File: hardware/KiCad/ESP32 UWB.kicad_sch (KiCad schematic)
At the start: 55 parts, among them J1 HEADER-20P-2.54, J2 HEADER-12P-2.54, J3 10118194-0001LF, Q1 S8050, Q2 S8050, SW1 BUTTON, SW2 BUTTON, U1 AMS1117-3.3, U2 ESP32-C3-MINI-1-N4, U3 SILICON_LABS_CP2102N-A01-GQFN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

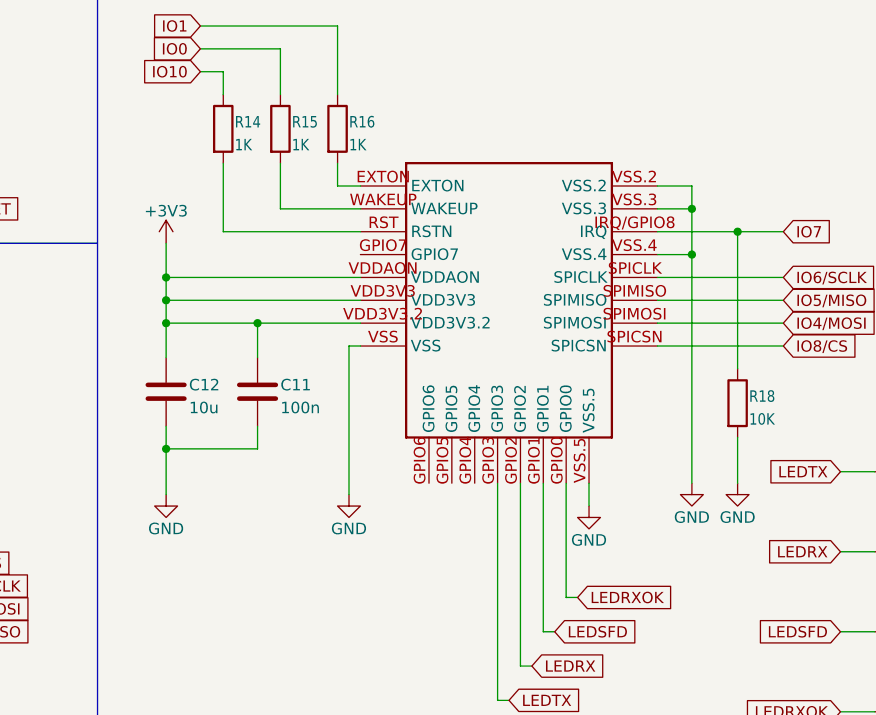
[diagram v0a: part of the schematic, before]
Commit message: further cleanup and improvment of the KiCad version of the PCB
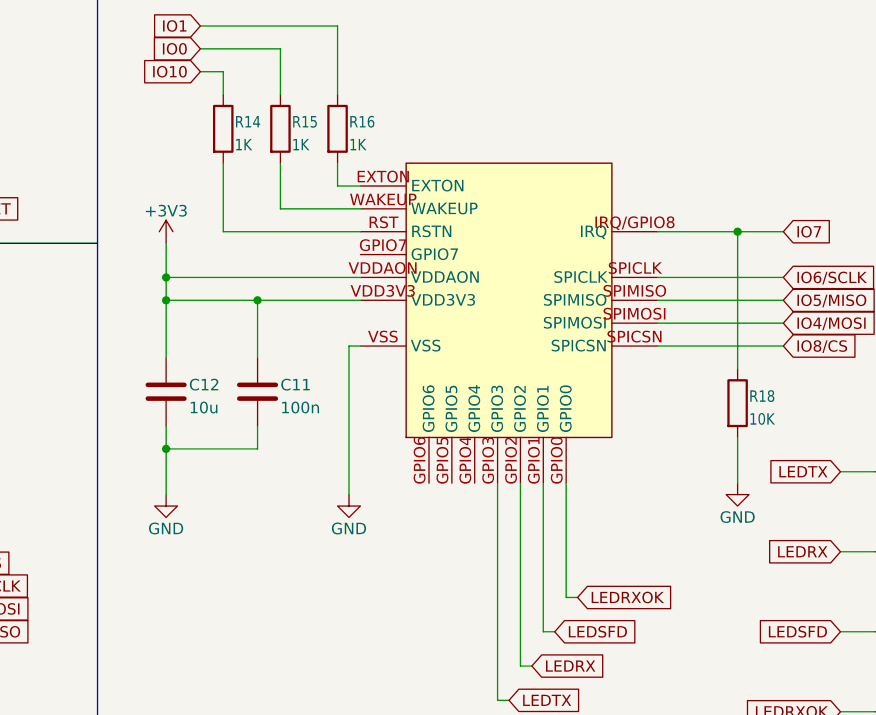
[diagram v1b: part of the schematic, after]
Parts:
- SW1, SW2: footprint Button_Switch_SMD:SW_SPST_EVQPE1 -> ESP32 UWB:SW_Push_3x4mm
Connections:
- net +3V3: no longer U4.VDD3V3.2
- net GND: no longer U4.VSS.2, U4.VSS.3, U4.VSS.4, U4.VSS.5
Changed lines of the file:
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@@
   (junction (at 173.99 123.19) (diameter 0) (color 0 0 0 0)
   )
-  (junction (at 297.18 135.89) (diameter 0) (color 0 0 0 0)
-  )
   (junction (at 146.05 171.45) (diameter 0) (color 0 0 0 0)
   )
@@
   (junction (at 151.13 41.91) (diameter 0) (color 0 0 0 0)
   )
-  (junction (at 238.76 146.05) (diameter 0) (color 0 0 0 0)
-  )
   (junction (at 193.04 113.03) (diameter 0) (color 0 0 0 0)
   )
@@
   (junction (at 173.99 107.95) (diameter 0) (color 0 0 0 0)
   )
-  (junction (at 238.76 148.59) (diameter 0) (color 0 0 0 0)
+  (junction (at 238.76 146.05) (diameter 0) (color 0 0 0 0)
   )
   (junction (at 316.23 50.8) (diameter 0) (color 0 0 0 0)
@@
   (junction (at 243.84 38.1) (diameter 0) (color 0 0 0 0)
   )
-  (junction (at 297.18 140.97) (diameter 0) (color 0 0 0 0)
-  )
   (junction (at 140.97 127) (diameter 0) (color 0 0 0 0)
   )
@@
   (junction (at 173.99 105.41) (diameter 0) (color 0 0 0 0)
   )
-  (junction (at 248.92 148.59) (diameter 0) (color 0 0 0 0)
+  (junction (at 248.92 146.05) (diameter 0) (color 0 0 0 0)
   )
   (junction (at 146.05 158.75) (diameter 0) (color 0 0 0 0)
@@
     (stroke (width 0) (type default) (color 0 0 0 0))
   )
-  (wire (pts (xy 238.76 152.4) (xy 238.76 148.59))
+  (wire (pts (xy 238.76 152.4) (xy 238.76 146.05))
     (stroke (width 0) (type default) (color 0 0 0 0))
   )
@@
     (stroke (width 0) (type default) (color 0 0 0 0))
   )
-  (wire (pts (xy 293.37 140.97) (xy 297.18 140.97))
-    (stroke (width 0) (type default) (color 0 0 0 0))
-  )
   (wire (pts (xy 161.29 110.49) (xy 173.99 110.49))
     (stroke (width 0) (type default) (color 0 0 0 0))
@@
     (stroke (width 0) (type default) (color 0 0 0 0))
   )
-  (wire (pts (xy 248.92 152.4) (xy 248.92 148.59))
+  (wire (pts (xy 248.92 152.4) (xy 248.92 146.05))
     (stroke (width 0) (type default) (color 0 0 0 0))
   )
@@
     (stroke (width 0) (type default) (color 0 0 0 0))
   )
-  (wire (pts (xy 238.76 146.05) (xy 238.76 143.51))
-    (stroke (width 0) (type default) (color 0 0 0 0))
-  )
   (wire (pts (xy 189.23 113.03) (xy 193.04 113.03))
     (stroke (width 0) (type default) (color 0 0 0 0))
@@
     (stroke (width 0) (type default) (color 0 0 0 0))
   )
-  (wire (pts (xy 297.18 140.97) (xy 297.18 135.89))
-    (stroke (width 0) (type default) (color 0 0 0 0))
-  )
   (wire (pts (xy 161.29 74.93) (xy 177.8 74.93))
     (stroke (width 0) (type default) (color 0 0 0 0))
@@
     (stroke (width 0) (type default) (color 0 0 0 0))
   )
-  (wire (pts (xy 238.76 148.59) (xy 248.92 148.59))
+  (wire (pts (xy 238.76 146.05) (xy 248.92 146.05))
     (stroke (width 0) (type default) (color 0 0 0 0))
   )
@@
     (stroke (width 0) (type default) (color 0 0 0 0))
   )
-  (wire (pts (xy 293.37 135.89) (xy 297.18 135.89))
-    (stroke (width 0) (type default) (color 0 0 0 0))
-  )
-  (wire (pts (xy 260.35 148.59) (xy 248.92 148.59))
-    (stroke (width 0) (type default) (color 0 0 0 0))
-  )
   (wire (pts (xy 302.26 138.43) (xy 302.26 153.67))
     (stroke (width 0) (type default) (color 0 0 0 0))
@@
     (stroke (width 0) (type default) (color 0 0 0 0))
   )
-  (wire (pts (xy 293.37 133.35) (xy 297.18 133.35))
-    (stroke (width 0) (type default) (color 0 0 0 0))
-  )
   (wire (pts (xy 308.61 71.12) (xy 317.5 71.12))
     (stroke (width 0) (type default) (color 0 0 0 0))
@@
     (stroke (width 0) (type default) (color 0 0 0 0))
   )
+  (wire (pts (xy 248.92 146.05) (xy 260.35 146.05))
+    (stroke (width 0) (type default) (color 0 0 0 0))
+  )
   (wire (pts (xy 199.39 77.47) (xy 215.9 77.47))
     (stroke (width 0) (type default) (color 0 0 0 0))
@@
     (stroke (width 0) (type default) (color 0 0 0 0))
   )
-  (wire (pts (xy 238.76 146.05) (xy 260.35 146.05))
-    (stroke (width 0) (type default) (color 0 0 0 0))
-  )
   (wire (pts (xy 259.08 151.13) (xy 260.35 151.13))
     (stroke (width 0) (type default) (color 0 0 0 0))
@@
     (stroke (width 0) (type default) (color 0 0 0 0))
   )
-  (wire (pts (xy 285.75 166.37) (xy 285.75 168.91))
-    (stroke (width 0) (type default) (color 0 0 0 0))
-  )
   (wire (pts (xy 85.09 160.02) (xy 97.79 160.02))
     (stroke (width 0) (type default) (color 0 0 0 0))
@@
     (stroke (width 0) (type default) (color 0 0 0 0))
   )
-  (wire (pts (xy 297.18 140.97) (xy 297.18 166.37))
-    (stroke (width 0) (type default) (color 0 0 0 0))
-  )
   (wire (pts (xy 251.46 135.89) (xy 260.35 135.89))
     (stroke (width 0) (type default) (color 0 0 0 0))
@@
     (stroke (width 0) (type default) (color 0 0 0 0))
   )
-  (wire (pts (xy 238.76 148.59) (xy 238.76 146.05))
+  (wire (pts (xy 238.76 143.51) (xy 238.76 146.05))
     (stroke (width 0) (type default) (color 0 0 0 0))
   )
@@
     (stroke (width 0) (type default) (color 0 0 0 0))
   )
-  (wire (pts (xy 297.18 135.89) (xy 297.18 133.35))
-    (stroke (width 0) (type default) (color 0 0 0 0))
-  )
   (wire (pts (xy 129.54 180.34) (xy 129.54 186.69))
     (stroke (width 0) (type default) (color 0 0 0 0))
@@
       (effects (font (size 1.778 1.5113)) (justify left bottom))
     )
-    (property "Footprint" "Button_Switch_SMD:SW_SPST_EVQPE1" (id 2) (at 102.87 173.99 0)
+    (property "Footprint" "ESP32 UWB:SW_Push_3x4mm" (id 2) (at 102.87 173.99 0)
       (effects (font (size 1.27 1.27)) hide)
     )
@@
       (effects (font (size 1.778 1.5113)) (justify left bottom))
     )
-    (property "Footprint" "Button_Switch_SMD:SW_SPST_EVQPE1" (id 2) (at 102.87 160.02 0)
+    (property "Footprint" "ESP32 UWB:SW_Push_3x4mm" (id 2) (at 102.87 160.02 0)
       (effects (font (size 1.27 1.27)) hide)
     )
@@
     (pin "SPIMOSI")
     (pin "VDD3V3")
-    (pin "VDD3V3.2")
     (pin "VDDAON")
     (pin "VSS")
-    (pin "VSS.2")
-    (pin "VSS.3")
-    (pin "VSS.4")
-    (pin "VSS.5")
     (pin "WAKEUP")
   )
@@
     (pin "1")
   )
-  (symbol (lib_id "power:GND") (at 285.75 168.91 0) (unit 1)
-    (in_bom yes) (on_board yes)
-    (property "Reference" "#PWR0112" (id 0) (at 285.75 175.26 0)
-      (effects (font (size 1.27 1.27)) hide)
-    )
-    (property "Value" "GND" (id 1) (at 285.75 172.72 0))
-    (property "Footprint" "" (id 2) (at 285.75 168.91 0)
-      (effects (font (size 1.27 1.27)) hide)
-    )
-    (property "Datasheet" "" (id 3) (at 285.75 168.91 0)
-      (effects (font (size 1.27 1.27)) hide)
-    )
-    (pin "1")
-  )
   (symbol (lib_id "Device:R") (at 321.31 165.1 90) (unit 1)
     (in_bom yes) (on_board yes)
@@
     (pin "2")
   )
-  (symbol (lib_id "power:GND") (at 297.18 166.37 0) (unit 1)
-    (in_bom yes) (on_board yes)
-    (property "Reference" "#PWR0114" (id 0) (at 297.18 172.72 0)
-      (effects (font (size 1.27 1.27)) hide)
-    )
-    (property "Value" "GND" (id 1) (at 297.18 170.18 0))
-    (property "Footprint" "" (id 2) (at 297.18 166.37 0)
-      (effects (font (size 1.27 1.27)) hide)
-    )
-    (property "Datasheet" "" (id 3) (at 297.18 166.37 0)
-      (effects (font (size 1.27 1.27)) hide)
-    )
-    (pin "1")
-  )
   (symbol (lib_id "Device:C") (at 259.08 44.45 0) (unit 1)
     (in_bom yes) (on_board yes)
@@
       (reference "#PWR0111") (unit 1) (value "GND") (footprint "")
     )
-    (path "/a66bd857-144e-4ab0-ab7a-3c10ed80cb1e"
-      (reference "#PWR0112") (unit 1) (value "GND") (footprint "")
-    )
     (path "/d6962950-4b71-4ba8-ac78-7b9bfb3edf70"
       (reference "#PWR0113") (unit 1) (value "GND") (footprint "")
     )
-    (path "/fc5e93f7-8264-46ce-a278-5944e151e5a7"
-      (reference "#PWR0114") (unit 1) (value "GND") (footprint "")
-    )
     (path "/a49f7437-7605-4a08-b3ab-0ea16e8bc6c8"
       (reference "#PWR0115") (unit 1) (value "GND") (footprint "")
@@
     )
     (path "/26769327-3160-41f1-82e7-11d5d542abde"
-      (reference "SW1") (unit 1) (value "BUTTON") (footprint "Button_Switch_SMD:SW_SPST_EVQPE1")
+      (reference "SW1") (unit 1) (value "BUTTON") (footprint "ESP32 UWB:SW_Push_3x4mm")
     )
     (path "/006bc43b-d3a8-4a38-a8dc-5a24da3f9b4d"
-      (reference "SW2") (unit 1) (value "BUTTON") (footprint "Button_Switch_SMD:SW_SPST_EVQPE1")
+      (reference "SW2") (unit 1) (value "BUTTON") (footprint "ESP32 UWB:SW_Push_3x4mm")
     )
     (path "/713f8bf8-d771-4862-bb18-7b6f3b027ba3"

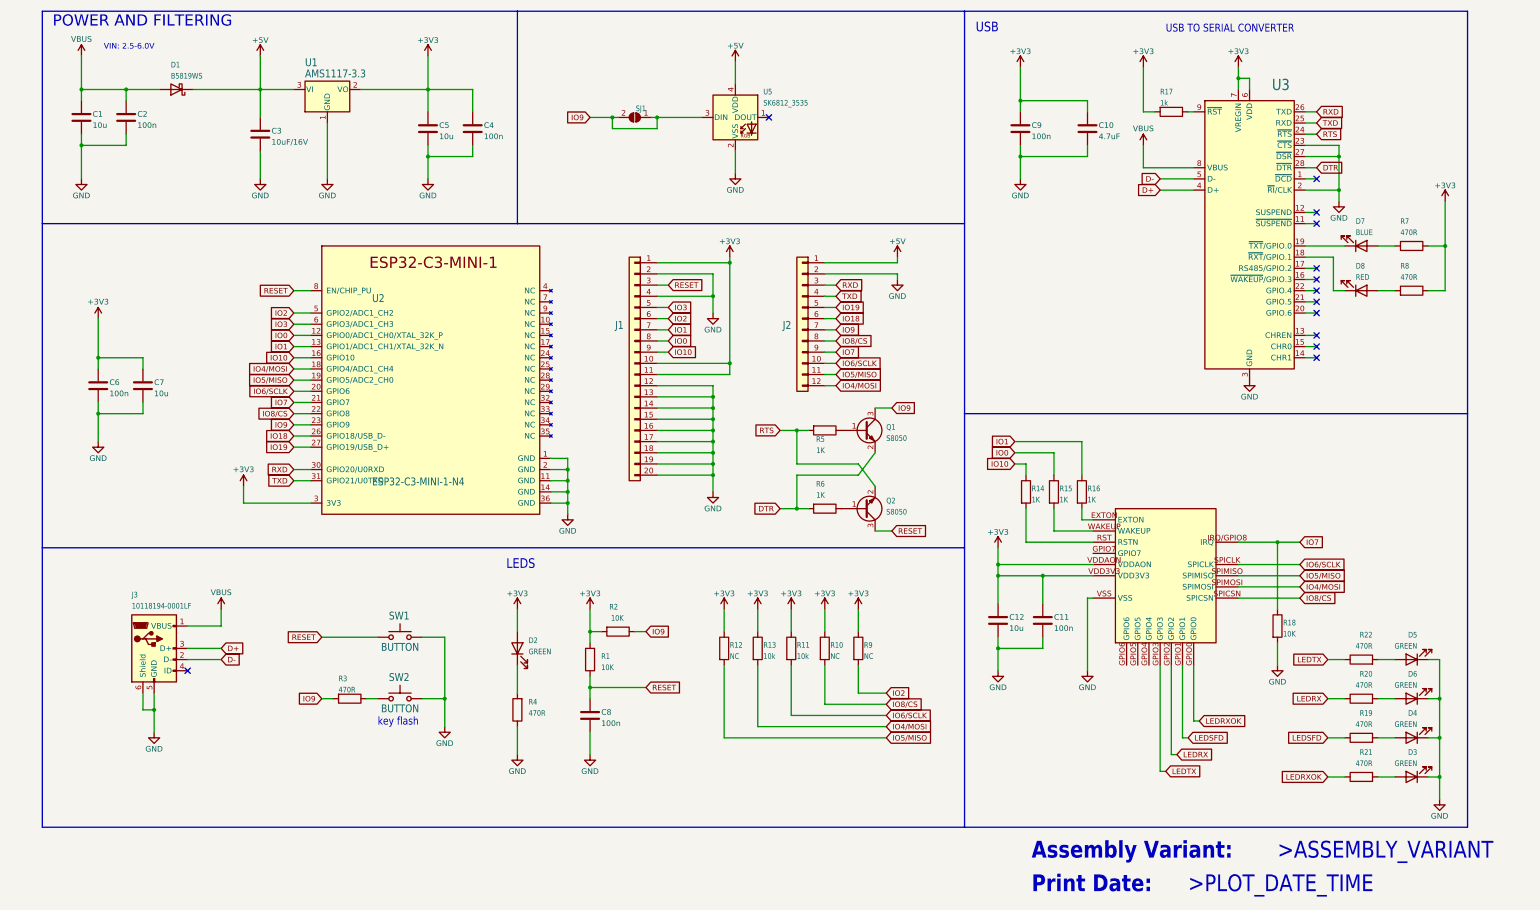
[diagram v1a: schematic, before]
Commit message: add BOM fields and tweak symbols and parts
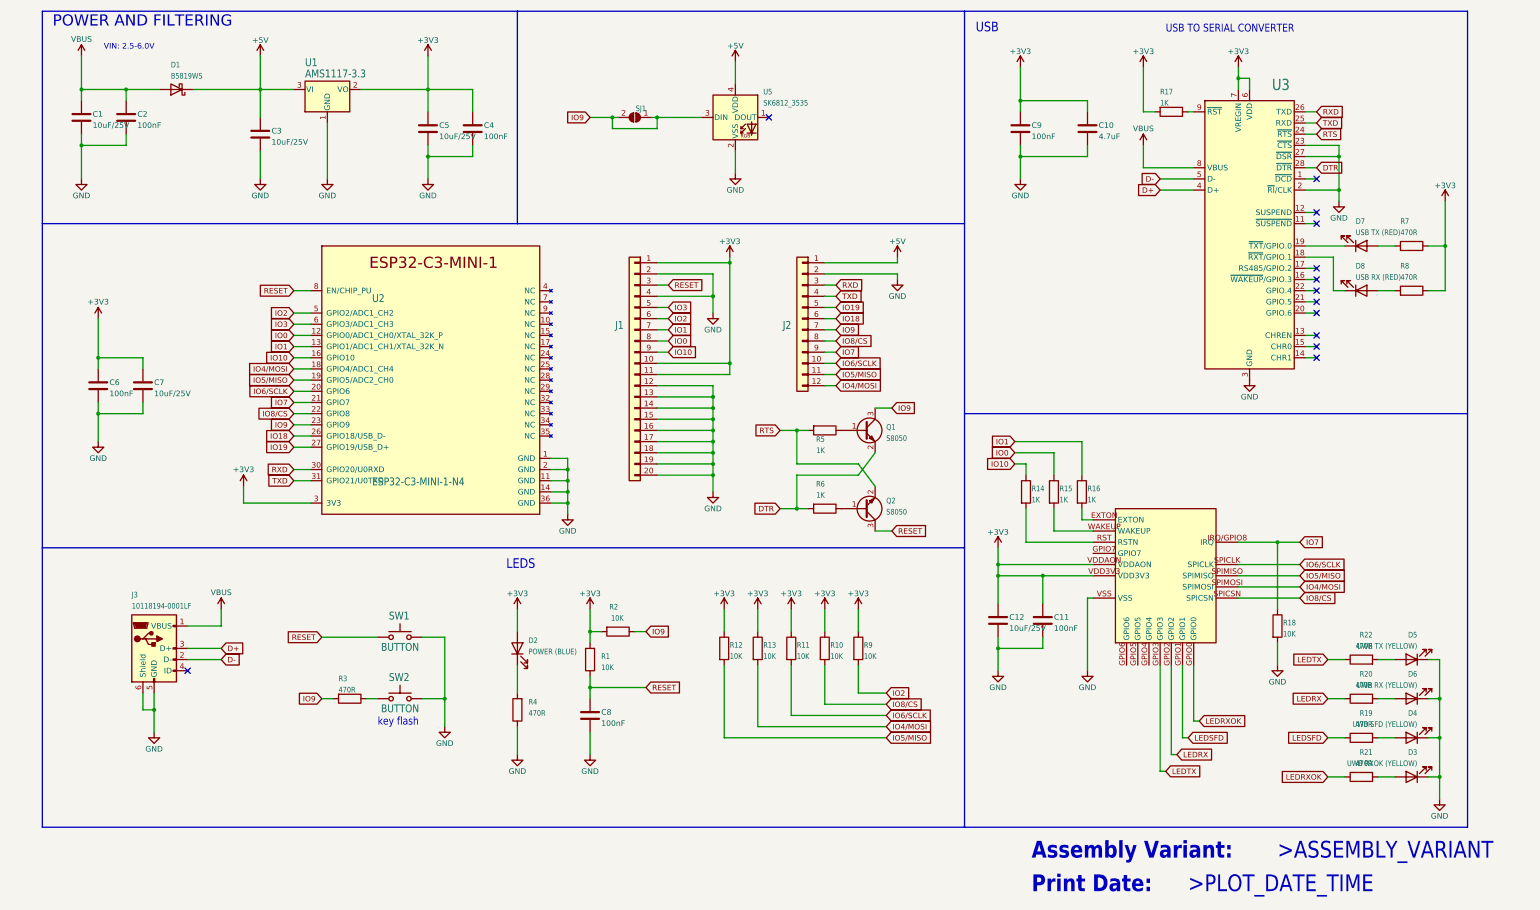
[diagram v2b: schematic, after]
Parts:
- C1, C12, C5, C7: value 10u -> 10uF/25V; Alternative (none) -> CL10X106MO8NRNC; LCSC (none) -> C96446
- C10: Alternative (none) -> CL10A475KO8NNNC; LCSC (none) -> C19666
- C11, C2, C4, C6, C8, C9: value 100n -> 100nF; Alternative (none) -> CL10B104KB8NNWC; LCSC (none) -> C14663
- C3: value 10uF/16V -> 10uF/25V; Alternative (none) -> CL10X106MO8NRNC; LCSC (none) -> C96446
- D1: Alternative (none) -> NSVR1020MW2T1G; LCSC (none) -> C191023
- D2: value GREEN -> POWER (BLUE); Alternative (none) -> 150080BS75000; LCSC (none) -> C2293
- D3: value GREEN -> UWB RXOK (YELLOW); Alternative (none) -> LY R976-PS-36; LCSC (none) -> C2296; Meaning RXDK -> RXOK
- D4: value GREEN -> UWB SFD (YELLOW); Alternative (none) -> LY R976-PS-36; LCSC (none) -> C2296
- D5: value GREEN -> UWB TX (YELLOW); Alternative (none) -> LY R976-PS-36; LCSC (none) -> C2296; Meaning (none) -> TX
- D6: value GREEN -> UWB RX (YELLOW); Alternative (none) -> LY R976-PS-36; LCSC (none) -> C2296
- D7: value BLUE -> USB TX (RED); Alternative (none) -> SML-D12U1WT86; LCSC (none) -> C2286
- D8: value RED -> USB RX (RED); Alternative (none) -> SML-D12U1WT86; LCSC (none) -> C2286
- J1: Alternative (none) -> PH1-20-UA; LCSC (none) -> C50981
- J2: Alternative (none) -> PH1-12-UA; LCSC (none) -> C225487
- J3: Alternative (none) -> 10118194-0001LF; LCSC (none) -> C132563
- Q1, Q2: Alternative (none) -> SS8050-G; LCSC (none) -> C2146
- R1, R18, R2: Alternative (none) -> RMCF0603JT10K0; LCSC (none) -> C25804
- R10, R12, R9: value NC -> 10K; Alternative (none) -> RMCF0603JT10K0; LCSC (none) -> C25804
- R11, R13: value 10k -> 10K; Alternative (none) -> RMCF0603JT10K0; LCSC (none) -> C25804
- R14, R15, R16, R5, R6: Alternative (none) -> RMCF0603JJ1K00; LCSC (none) -> C21190
- R17: value 1k -> 1K; Alternative (none) -> RMCF0603JJ1K00; LCSC (none) -> C21190
- R19, R20, R21, R22, R3, R4, R7, R8: Alternative (none) -> RMCF0603JT470R; LCSC (none) -> C23179
- SJ1: now left out of the parts list
- SW1, SW2: Alternative (none) -> PTS820J15MSMTRLFS; LCSC (none) -> C720477
- U1: Alternative (none) -> NCP1117LPST33T3G; Comment (none) -> Uncommon Pinout for SOT-223 LDOs!; LCSC (none) -> C6186
- U2: Alternative (none) -> ESP32-C3-MINI-1-N4; LCSC (none) -> C2838502
- U3: Alternative (none) -> CP2102N-A02-GQFN28; LCSC (none) -> C6568
- U4: value DWM1000 -> BU01; footprint ESP32 UWB:DWM1000 -> ESP32 UWB:BU01; symbol ESP32 UWB-eagle-import:DWM1000 -> ESP32 UWB:BU01; Alternative (none) -> BU01; LCSC (none) -> C503604
- U5: Alternative (none) -> SK6812 3535; Comment (none) -> also Adafruit #2659/#2686 and Aliexpress

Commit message: tweak bom some more
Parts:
- C1, C12, C3, C5, C7: Alternative CL10X106MO8NRNC -> (none); Part (none) -> CL10X106MO8NRNC
- C10: Alternative CL10A475KO8NNNC -> (none); Part (none) -> CL10A475KO8NNNC
- C11, C2, C4, C6, C8, C9: Alternative CL10B104KB8NNWC -> (none); Part (none) -> CL10B104KB8NNWC
- D1: Alternative NSVR1020MW2T1G -> (none); Part (none) -> NSVR1020MW2T1G
- D2: Alternative 150080BS75000 -> (none); Part (none) -> 150080BS75000
- D3, D4, D5, D6: Alternative LY R976-PS-36 -> (none); Part (none) -> LY R976-PS-36
- D7, D8: Alternative SML-D12U1WT86 -> (none); Part (none) -> SML-D12U1WT86
- J1: Alternative PH1-20-UA -> (none); Part (none) -> PH1-20-UA
- J2: Alternative PH1-12-UA -> (none); Part (none) -> PH1-12-UA
- J3: Alternative 10118194-0001LF -> (none); Part (none) -> 10118194-0001LF
- Q1, Q2: Alternative SS8050-G -> (none); Part (none) -> SS8050-G
- R1, R10, R11, R12, R13, R18, R2, R9: Alternative RMCF0603JT10K0 -> (none); Part (none) -> RMCF0603JT10K0
- R14, R15, R16, R17, R5, R6: Alternative RMCF0603JJ1K00 -> (none); Part (none) -> RMCF0603JJ1K00
- R19, R20, R21, R22, R3, R4, R7, R8: Alternative RMCF0603JT470R -> (none); Part (none) -> RMCF0603JT470R
- SW1, SW2: Alternative PTS820J15MSMTRLFS -> (none); Part (none) -> PTS820J15MSMTRLFS
- U1: Alternative NCP1117LPST33T3G -> (none); Part (none) -> NCP1117LPST33T3G
- U2: Alternative ESP32-C3-MINI-1-N4 -> (none); Part (none) -> ESP32-C3-MINI-1-N4
- U3: Alternative CP2102N-A02-GQFN28 -> (none); Part (none) -> CP2102N-A02-GQFN28
- U4: Alternative BU01 -> (none); Comment (none) -> AliExpress; Part (none) -> BU01
- U5: Alternative SK6812 3535 -> (none); Comment also Adafruit #2659/#2686 and Aliexpress -> optional, search "SK6812 3535" on Aliexpress, also Adafruit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; Part (none) -> 2659
